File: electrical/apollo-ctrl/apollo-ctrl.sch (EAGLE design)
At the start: 61 parts, among them Q1 N-chan, Q2 N-chan, U1 NANO, U2 ADAFRUIT-MPRLS, X1 BARREL-JACK, X2 SENSOR-O2

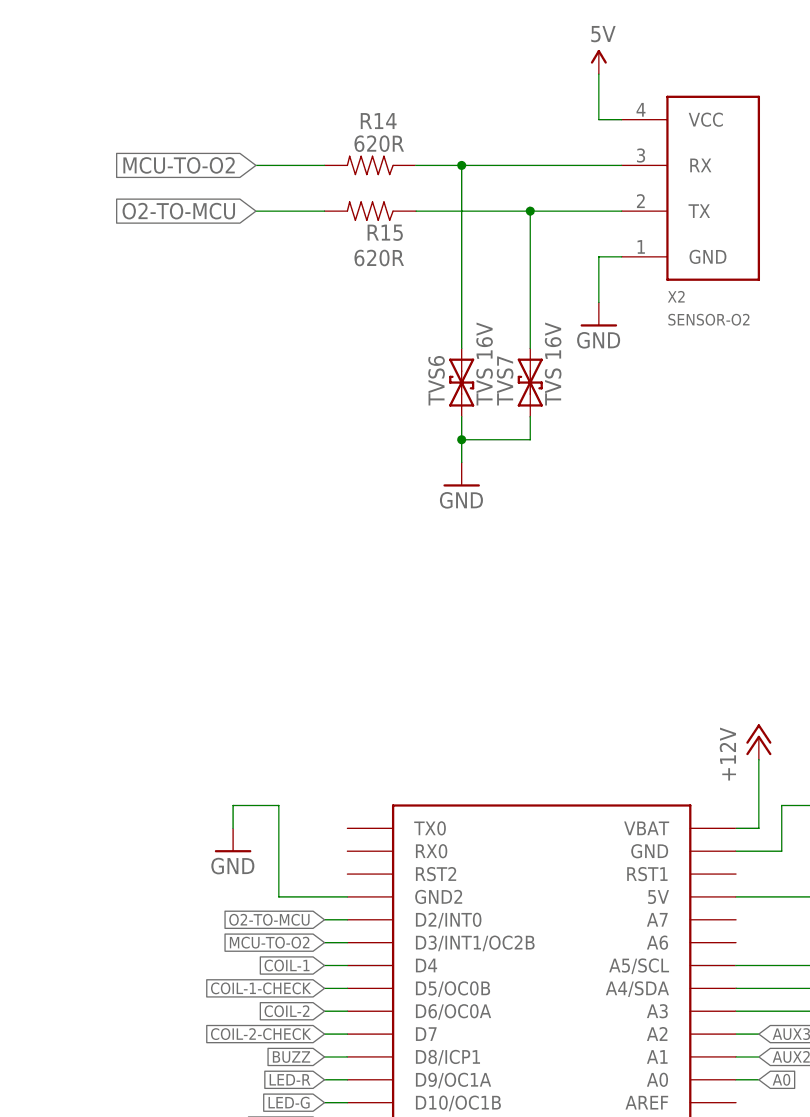
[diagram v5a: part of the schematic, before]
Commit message: all components now top side
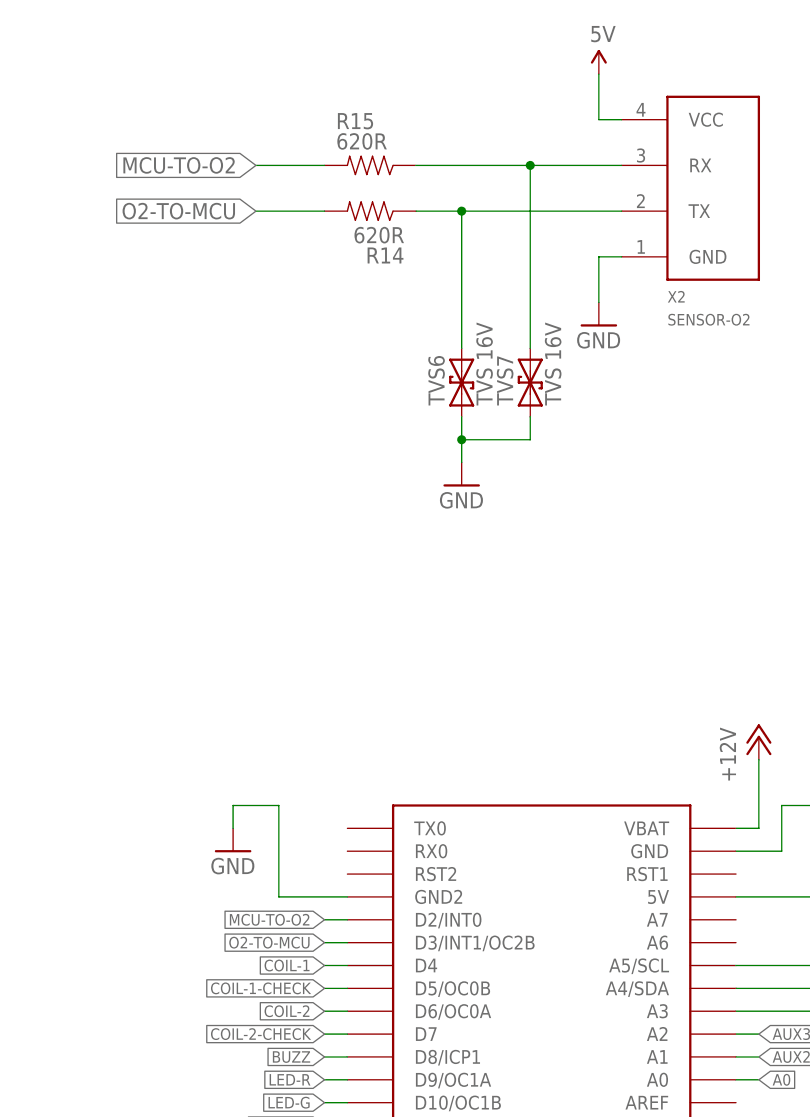
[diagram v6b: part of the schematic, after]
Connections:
- net MCU-TO-O2: now also R15.2, U1.D2/INT0; no longer R14.2, U1.D3/INT1/OC2B
- net N$17: now also X2.TX; no longer X2.RX
- net N$18: now also X2.RX; no longer X2.TX
- net O2-TO-MCU: now also R14.2, U1.D3/INT1/OC2B; no longer R15.2, U1.D2/INT0
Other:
- moved on the sheet: R14, R15
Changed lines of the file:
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@@
 <attribute name="VALUE" x="35.56" y="111.76" size="1.778" layer="96"/>
 </instance>
-<instance part="R15" gate="G$1" x="12.7" y="127" smashed="yes" rot="R180">
-<attribute name="NAME" x="16.51" y="125.5014" size="1.778" layer="95" rot="R180"/>
-<attribute name="VALUE" x="16.51" y="122.682" size="1.778" layer="96" rot="R180"/>
-</instance>
-<instance part="R14" gate="G$1" x="12.7" y="132.08" smashed="yes" rot="R180">
-<attribute name="NAME" x="11.43" y="136.1186" size="1.778" layer="95"/>
-<attribute name="VALUE" x="16.51" y="135.382" size="1.778" layer="96" rot="R180"/>
+<instance part="R15" gate="G$1" x="12.7" y="132.08" smashed="yes" rot="R180">
+<attribute name="NAME" x="8.89" y="136.1186" size="1.778" layer="95"/>
+<attribute name="VALUE" x="8.89" y="133.858" size="1.778" layer="96"/>
+</instance>
+<instance part="R14" gate="G$1" x="12.7" y="127" smashed="yes" rot="R180">
+<attribute name="NAME" x="16.51" y="122.9614" size="1.778" layer="95" rot="R180"/>
+<attribute name="VALUE" x="16.51" y="125.222" size="1.778" layer="96" rot="R180"/>
 </instance>
 <instance part="P+8" gate="G$1" x="38.1" y="142.24" smashed="yes">
@@
 <net name="N$17" class="0">
 <segment>
+<pinref part="R14" gate="G$1" pin="1"/>
+<pinref part="TVS6" gate="G$1" pin="C"/>
+<wire x1="22.86" y1="127" x2="17.78" y2="127" width="0.1524" layer="91"/>
+<wire x1="22.86" y1="111.76" x2="22.86" y2="127" width="0.1524" layer="91"/>
+<pinref part="X2" gate="G$1" pin="TX"/>
+<wire x1="22.86" y1="127" x2="40.64" y2="127" width="0.1524" layer="91"/>
+<junction x="22.86" y="127"/>
+</segment>
+</net>
+<net name="N$18" class="0">
+<segment>
+<pinref part="R15" gate="G$1" pin="1"/>
+<pinref part="TVS7" gate="G$1" pin="C"/>
+<wire x1="30.48" y1="132.08" x2="17.78" y2="132.08" width="0.1524" layer="91"/>
+<wire x1="30.48" y1="111.76" x2="30.48" y2="132.08" width="0.1524" layer="91"/>
 <pinref part="X2" gate="G$1" pin="RX"/>
-<pinref part="R14" gate="G$1" pin="1"/>
-<wire x1="40.64" y1="132.08" x2="22.86" y2="132.08" width="0.1524" layer="91"/>
-<pinref part="TVS6" gate="G$1" pin="C"/>
-<wire x1="22.86" y1="132.08" x2="17.78" y2="132.08" width="0.1524" layer="91"/>
-<wire x1="22.86" y1="111.76" x2="22.86" y2="132.08" width="0.1524" layer="91"/>
-<junction x="22.86" y="132.08"/>
-</segment>
-</net>
-<net name="N$18" class="0">
-<segment>
-<pinref part="X2" gate="G$1" pin="TX"/>
-<pinref part="R15" gate="G$1" pin="1"/>
-<wire x1="40.64" y1="127" x2="30.48" y2="127" width="0.1524" layer="91"/>
-<pinref part="TVS7" gate="G$1" pin="C"/>
-<wire x1="30.48" y1="127" x2="17.78" y2="127" width="0.1524" layer="91"/>
-<wire x1="30.48" y1="111.76" x2="30.48" y2="127" width="0.1524" layer="91"/>
-<junction x="30.48" y="127"/>
+<wire x1="30.48" y1="132.08" x2="40.64" y2="132.08" width="0.1524" layer="91"/>
+<junction x="30.48" y="132.08"/>
 </segment>
 </net>
@@
 </segment>
 </net>
-<net name="MCU-TO-O2" class="0">
+<net name="O2-TO-MCU" class="0">
 <segment>
 <pinref part="R14" gate="G$1" pin="2"/>
-<wire x1="7.62" y1="132.08" x2="0" y2="132.08" width="0.1524" layer="91"/>
-<label x="0" y="132.08" size="1.778" layer="95" rot="R180" xref="yes"/>
+<wire x1="7.62" y1="127" x2="0" y2="127" width="0.1524" layer="91"/>
+<label x="0" y="127" size="1.778" layer="95" rot="R180" xref="yes"/>
 </segment>
 <segment>
@@
 </segment>
 </net>
-<net name="O2-TO-MCU" class="0">
+<net name="MCU-TO-O2" class="0">
 <segment>
 <pinref part="R15" gate="G$1" pin="2"/>
-<wire x1="7.62" y1="127" x2="0" y2="127" width="0.1524" layer="91"/>
-<label x="0" y="127" size="1.778" layer="95" rot="R180" xref="yes"/>
-</segment>
-<segment>
+<wire x1="7.62" y1="132.08" x2="0" y2="132.08" width="0.1524" layer="91"/>
+<label x="0" y="132.08" size="1.778" layer="95" rot="R180" xref="yes"/>
+</segment>
+<segment>

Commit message: added a fan header
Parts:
- added X4: FAN, apollo-ctrl:M02PTH
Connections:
- net +12V: now also X4.1
- net GND: now also X4.2
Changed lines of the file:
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@@
 <part name="SJ1" library="apollo-ctrl" deviceset="SOLDERJUMPER" device="NO" value=""/>
 <part name="SJ2" library="apollo-ctrl" deviceset="SOLDERJUMPER" device="NO" value=""/>
+<part name="X4" library="apollo-ctrl" deviceset="M02" device="PTH" value="FAN"/>
+<part name="GND32" library="apollo-ctrl" deviceset="GND" device=""/>
+<part name="P+12" library="apollo-ctrl" deviceset="+12V" device=""/>
 </parts>
 <sheets>
@@
 <instance part="SJ1" gate="1" x="134.62" y="116.84" rot="R90"/>
 <instance part="SJ2" gate="1" x="121.92" y="116.84" rot="R90"/>
+<instance part="X4" gate="G$1" x="172.72" y="2.54" rot="R180"/>
+<instance part="GND32" gate="1" x="162.56" y="-5.08" smashed="yes">
+<attribute name="VALUE" x="160.02" y="-7.62" size="1.778" layer="96"/>
+</instance>
+<instance part="P+12" gate="1" x="162.56" y="7.62" smashed="yes">
+<attribute name="VALUE" x="160.02" y="2.54" size="1.778" layer="96" rot="R90"/>
+</instance>
 </instances>
 <busses>
@@
 <pinref part="X3" gate="G$1" pin="8"/>
 <wire x1="152.4" y1="48.26" x2="165.1" y2="48.26" width="0.1524" layer="91"/>
+</segment>
+<segment>
+<pinref part="X4" gate="G$1" pin="2"/>
+<wire x1="165.1" y1="0" x2="162.56" y2="0" width="0.1524" layer="91"/>
+<pinref part="GND32" gate="1" pin="GND"/>
+<wire x1="162.56" y1="0" x2="162.56" y2="-2.54" width="0.1524" layer="91"/>
 </segment>
 </net>
@@
 <junction x="-53.34" y="66.04"/>
 </segment>
-</net>
+<segment>
+<pinref part="X4" gate="G$1" pin="1"/>
+<wire x1="165.1" y1="2.54" x2="162.56" y2="2.54" width="0.1524" layer="91"/>
+<pinref part="P+12" gate="1" pin="+12V"/>
+<wire x1="162.56" y1="2.54" x2="162.56" y2="5.08" width="0.1524" layer="91"/>
+</segment>
+</net>

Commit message: minor tweaks for ctrl pcb before fab
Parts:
- added SG2, SG3, SG4: BUZZER, apollo-ctrl:M01-TH-NS
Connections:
- net BUZZ: now also SG2.1, SG3.1, SG4.1
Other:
- note added: "poor-man's battery charger treats the battery like a super-cap use Li-Ion only! 14500 cell 2.8V to 4.2V"
- note removed: "poor-man's battery charger treats the battery like a super-cap use Li-Ion only! 14500 cell"
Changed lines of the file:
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@@
 <layer number="54" name="bGND_GNDA" color="1" fill="9" visible="yes" active="no"/>
 <layer number="56" name="wert" color="7" fill="1" visible="yes" active="no"/>
+<layer number="57" name="tCAD" color="7" fill="1" visible="yes" active="no"/>
+<layer number="59" name="tCarbon" color="7" fill="1" visible="yes" active="no"/>
+<layer number="60" name="bCarbon" color="7" fill="1" visible="yes" active="no"/>
 <layer number="88" name="SimResults" color="9" fill="1" visible="yes" active="yes"/>
 <layer number="89" name="SimProbes" color="9" fill="1" visible="yes" active="yes"/>
@@
 <layer number="106" name="bPlate" color="7" fill="1" visible="no" active="yes"/>
 <layer number="107" name="Crop" color="7" fill="1" visible="no" active="yes"/>
+<layer number="108" name="tBridges" color="7" fill="1" visible="yes" active="yes"/>
+<layer number="109" name="tBPL" color="7" fill="1" visible="yes" active="yes"/>
+<layer number="110" name="bBPL" color="7" fill="1" visible="yes" active="yes"/>
+<layer number="111" name="MPL" color="7" fill="1" visible="yes" active="yes"/>
+<layer number="112" name="tSilk" color="7" fill="1" visible="yes" active="yes"/>
+<layer number="113" name="ReferenceLS" color="7" fill="1" visible="yes" active="yes"/>
+<layer number="114" name="tPlaceRed" color="7" fill="1" visible="yes" active="yes"/>
+<layer number="115" name="FRNTMAAT2" color="7" fill="1" visible="yes" active="yes"/>
 <layer number="116" name="Patch_BOT" color="9" fill="4" visible="no" active="yes"/>
+<layer number="117" name="BACKMAAT1" color="7" fill="1" visible="yes" active="yes"/>
+<layer number="118" name="Rect_Pads" color="7" fill="1" visible="yes" active="yes"/>
+<layer number="119" name="KAP_TEKEN" color="7" fill="1" visible="yes" active="yes"/>
+<layer number="120" name="KAP_MAAT1" color="7" fill="1" visible="yes" active="yes"/>
 <layer number="121" name="_tsilk" color="7" fill="1" visible="no" active="yes"/>
 <layer number="122" name="_bsilk" color="7" fill="1" visible="no" active="yes"/>
+<layer number="123" name="tTestmark" color="7" fill="1" visible="yes" active="yes"/>
+<layer number="124" name="bTestmark" color="7" fill="1" visible="yes" active="yes"/>
 <layer number="125" name="_tNames" color="7" fill="1" visible="no" active="yes"/>
 <layer number="126" name="_bNames" color="7" fill="1" visible="yes" active="yes"/>
 <layer number="127" name="_tValues" color="7" fill="1" visible="yes" active="yes"/>
 <layer number="128" name="_bValues" color="7" fill="1" visible="yes" active="yes"/>
+<layer number="129" name="Mask" color="7" fill="1" visible="yes" active="yes"/>
+<layer number="130" name="SMDSTROOK" color="7" fill="1" visible="yes" active="yes"/>
+<layer number="131" name="tAdjust" color="7" fill="1" visible="yes" active="yes"/>
+<layer number="132" name="bAdjust" color="7" fill="1" visible="yes" active="yes"/>
+<layer number="133" name="bottom_silk" color="7" fill="1" visible="yes" active="yes"/>
 <layer number="144" name="Drill_legend" color="7" fill="1" visible="no" active="yes"/>
+<layer number="150" name="Notes" color="7" fill="1" visible="yes" active="yes"/>
 <layer number="151" name="HeatSink" color="7" fill="1" visible="no" active="yes"/>
 <layer number="152" name="_bDocu" color="7" fill="1" visible="yes" active="yes"/>
+<layer number="153" name="FabDoc1" color="7" fill="1" visible="yes" active="yes"/>
+<layer number="154" name="FabDoc2" color="7" fill="1" visible="yes" active="yes"/>
+<layer number="155" name="FabDoc3" color="7" fill="1" visible="yes" active="yes"/>
+<layer number="199" name="Contour" color="7" fill="1" visible="yes" active="yes"/>
 <layer number="200" name="200bmp" color="1" fill="10" visible="no" active="yes"/>
 <layer number="201" name="201bmp" color="2" fill="10" visible="no" active="yes"/>
@@
 <layer number="223" name="223bmp" color="24" fill="1" visible="no" active="no"/>
 <layer number="224" name="224bmp" color="25" fill="1" visible="no" active="no"/>
+<layer number="225" name="225bmp" color="7" fill="1" visible="yes" active="yes"/>
+<layer number="226" name="226bmp" color="7" fill="1" visible="yes" active="yes"/>
+<layer number="227" name="227bmp" color="7" fill="1" visible="yes" active="yes"/>
+<layer number="228" name="228bmp" color="7" fill="1" visible="yes" active="yes"/>
+<layer number="229" name="229bmp" color="7" fill="1" visible="yes" active="yes"/>
+<layer number="230" name="230bmp" color="7" fill="1" visible="yes" active="yes"/>
+<layer number="231" name="Eagle3D_PG1" color="7" fill="1" visible="yes" active="yes"/>
+<layer number="232" name="Eagle3D_PG2" color="7" fill="1" visible="yes" active="yes"/>
+<layer number="233" name="Eagle3D_PG3" color="7" fill="1" visible="yes" active="yes"/>
+<layer number="248" name="Housing" color="7" fill="1" visible="yes" active="yes"/>
+<layer number="249" name="Edge" color="7" fill="1" visible="yes" active="yes"/>
 <layer number="250" name="Descript" color="3" fill="1" visible="no" active="no"/>
 <layer number="251" name="SMDround" color="12" fill="11" visible="no" active="no"/>
 <layer number="254" name="cooling" color="7" fill="1" visible="no" active="yes"/>
+<layer number="255" name="routoute" color="7" fill="1" visible="yes" active="yes"/>
 </layers>
 <schematic xreflabel="%F%N/%S.%C%R" xrefpart="/%S.%C%R">
@@
 </part>
 <part name="D9" library="apollo-ctrl" deviceset="DIODE" device="1N4148"/>
-<part name="D5" library="apollo-ctrl" deviceset="DIODE-SCHOTTKY" device="PTH" value=""/>
-<part name="D4" library="apollo-ctrl" deviceset="DIODE-SCHOTTKY" device="PTH" value=""/>
+<part name="D5" library="apollo-ctrl" deviceset="DIODE-SCHOTTKY" device="PTH" value="DIODE-SCHOTTKYPTH"/>
+<part name="D4" library="apollo-ctrl" deviceset="DIODE-SCHOTTKY" device="PTH" value="DIODE-SCHOTTKYPTH"/>
 <part name="P+1" library="apollo-ctrl" deviceset="+12V" device=""/>
 <part name="GND1" library="apollo-ctrl" deviceset="GND" device=""/>
@@
 <part name="GND28" library="apollo-ctrl" deviceset="GND" device=""/>
 <part name="P+5" library="apollo-ctrl" deviceset="3.3V" device=""/>
-<part name="D2" library="apollo-ctrl" deviceset="DIODE-SCHOTTKY" device="PTH" value=""/>
+<part name="D2" library="apollo-ctrl" deviceset="DIODE-SCHOTTKY" device="PTH" value="DIODE-SCHOTTKYPTH"/>
 <part name="D1" library="apollo-ctrl" deviceset="DIODE-ZENER" device="1N4148" value="3V6"/>
 <part name="R1" library="apollo-ctrl" deviceset="RESISTOR" device="PTH-1/2W" value="470R 500mW"/>
@@
 <part name="GND32" library="apollo-ctrl" deviceset="GND" device=""/>
 <part name="P+12" library="apollo-ctrl" deviceset="+12V" device=""/>
+<part name="SG2" library="apollo-ctrl" deviceset="M01" device="-TH-NS" value="BUZZER"/>
+<part name="SG3" library="apollo-ctrl" deviceset="M01" device="-TH-NS" value="BUZZER"/>
+<part name="SG4" library="apollo-ctrl" deviceset="M01" device="-TH-NS" value="BUZZER"/>
 </parts>
 <sheets>
@@
 <text x="-139.7" y="71.12" size="1.778" layer="97">poor-man's battery charger
 treats the battery like a super-cap
-use Li-Ion only! 14500 cell</text>
+use Li-Ion only! 14500 cell
+2.8V to 4.2V</text>
 <text x="-53.34" y="-48.26" size="1.778" layer="97">continuity checker</text>
 <text x="-58.42" y="15.24" size="1.778" layer="97">power fail detection</text>
@@
 <attribute name="VALUE" x="160.02" y="2.54" size="1.778" layer="96" rot="R90"/>
 </instance>
+<instance part="SG2" gate="G$1" x="-40.64" y="144.78" rot="R180"/>
+<instance part="SG3" gate="G$1" x="-40.64" y="157.48" rot="R180"/>
+<instance part="SG4" gate="G$1" x="-40.64" y="170.18" rot="R180"/>
 </instances>
 <busses>
@@
 <label x="7.62" y="33.02" size="1.27" layer="95" rot="R180" xref="yes"/>
 </segment>
-</net>
+<segment>
+<pinref part="SG4" gate="G$1" pin="1"/>
+<wire x1="-48.26" y1="170.18" x2="-50.8" y2="170.18" width="0.1524" layer="91"/>
+<wire x1="-50.8" y1="170.18" x2="-50.8" y2="157.48" width="0.1524" layer="91"/>
+<pinref part="SG3" gate="G$1" pin="1"/>
+<wire x1="-50.8" y1="157.48" x2="-48.26" y2="157.48" width="0.1524" layer="91"/>
+<pinref part="SG2" gate="G$1" pin="1"/>
+<wire x1="-48.26" y1="144.78" x2="-50.8" y2="144.78" width="0.1524" layer="91"/>
+<wire x1="-50.8" y1="144.78" x2="-50.8" y2="157.48" width="0.1524" layer="91"/>
+<wire x1="-50.8" y1="144.78" x2="-53.34" y2="144.78" width="0.1524" layer="91"/>
+<label x="-53.34" y="144.78" size="1.27" layer="95" rot="R180" xref="yes"/>
+<junction x="-50.8" y="144.78"/>
+<junction x="-50.8" y="157.48"/>
+</segment>
+</net>
